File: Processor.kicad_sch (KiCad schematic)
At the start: 36 parts, among them J5 GPIO, SW2 SW_Push, U12 8086_Max_Mode, U13 8284, U14 8087, U15 8089, U16 80130-6, U17 8288, U18 8289, U19 74LS573, U20 74LS245, U21 74LS573, U22 74LS245, U23 74LS573, U24 74LS06, U26 74LS273, U27 74LS273, U28 74LS244, U29 74LS244, U30 74LS32, Y1 15MHz

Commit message: Adjusted Data Bus for 80130
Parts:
- removed unit 3 of U24
- added U34: 74HC00, Package_DIP:DIP-14_W7.62mm, symbol 74xx:74HC00
- J5: footprint (none) -> Connector_PinHeader_2.54mm:PinHeader_2x08_P2.54mm_Vertical
- U15: footprint (none) -> Package_DIP:DIP-40_W15.24mm
- U16: footprint (none) -> Package_DIP:DIP-40_W15.24mm_Socket
- U18, U21, U22, U23, U26, U27, U28: footprint (none) -> Package_DIP:DIP-20_W7.62mm
- U24, U30: footprint (none) -> Package_DIP:DIP-14_W7.62mm
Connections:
- net 5V-18: now also U34.14 (VCC)
- net DEN: now also U34.1
- net GND: now also U34.10, U34.12, U34.13, U34.4, U34.5, U34.7 (GND), U34.9
- net ~{DEN}: now also U34.3
- net ~{LIR}: now reaches U16.24 (~{LIR})
- net ~{ACK}: now reaches U16.25 (~{ACK})
- net ~{ACK}: now also U34.2
- net RDY2: no longer names the net of RN1.3 (R2)
- net RDY2: no longer U13.6 (RDY2)
- new net IORDY: U13.6 (RDY2)

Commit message: assigned all footprints
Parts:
- C3: footprint (none) -> Capacitor_THT:CP_Radial_D6.3mm_P2.50mm
- C4: footprint (none) -> Capacitor_THT:C_Disc_D8.0mm_W2.5mm_P5.00mm
- JP2, JP3, JP4, JP6: footprint (none) -> Connector_PinHeader_2.54mm:PinHeader_1x02_P2.54mm_Vertical
- R3, R4, R5, R6, R7: footprint (none) -> Resistor_THT:R_Axial_DIN0207_L6.3mm_D2.5mm_P7.62mm_Horizontal
- SW2: footprint (none) -> Button_Switch_THT:SW_PUSH_6mm
- U19, U20, U29: footprint (none) -> Package_DIP:DIP-20_W7.62mm
- Y1: footprint (none) -> Crystal:Crystal_HC49-U_Vertical
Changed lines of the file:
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@@
 			)
 		)
-		(property "Footprint" ""
+		(property "Footprint" "Connector_PinHeader_2.54mm:PinHeader_1x02_P2.54mm_Vertical"
 			(at 176.53 194.31 0)
 			(effects
@@
 			)
 		)
-		(property "Footprint" ""
+		(property "Footprint" "Connector_PinHeader_2.54mm:PinHeader_1x02_P2.54mm_Vertical"
 			(at 62.23 114.3 0)
 			(effects
@@
 			)
 		)
-		(property "Footprint" ""
+		(property "Footprint" "Resistor_THT:R_Axial_DIN0207_L6.3mm_D2.5mm_P7.62mm_Horizontal"
 			(at 84.582 30.48 90)
 			(effects
@@
 			)
 		)
-		(property "Footprint" ""
+		(property "Footprint" "Capacitor_THT:C_Disc_D8.0mm_W2.5mm_P5.00mm"
 			(at 65.7352 66.04 0)
 			(effects
@@
 			)
 		)
-		(property "Footprint" ""
+		(property "Footprint" "Resistor_THT:R_Axial_DIN0207_L6.3mm_D2.5mm_P7.62mm_Horizontal"
 			(at 22.352 107.95 90)
 			(effects
@@
 			)
 		)
-		(property "Footprint" ""
+		(property "Footprint" "Connector_PinHeader_2.54mm:PinHeader_1x02_P2.54mm_Vertical"
 			(at 162.2817 212.09 0)
 			(effects
@@
 			)
 		)
-		(property "Footprint" ""
+		(property "Footprint" "Button_Switch_THT:SW_PUSH_6mm"
 			(at 81.28 29.21 0)
 			(effects
@@
 			)
 		)
-		(property "Footprint" ""
+		(property "Footprint" "Crystal:Crystal_HC49-U_Vertical"
 			(at 64.77 69.85 0)
 			(effects
@@
 			)
 		)
-		(property "Footprint" ""
+		(property "Footprint" "Package_DIP:DIP-20_W7.62mm"
 			(at 38.1 166.37 0)
 			(effects
@@
 			)
 		)
-		(property "Footprint" ""
+		(property "Footprint" "Resistor_THT:R_Axial_DIN0207_L6.3mm_D2.5mm_P7.62mm_Horizontal"
 			(at 32.512 107.95 90)
 			(effects
@@
 			)
 		)
-		(property "Footprint" ""
+		(property "Footprint" "Connector_PinHeader_2.54mm:PinHeader_1x02_P2.54mm_Vertical"
 			(at 245.11 118.11 0)
 			(effects
@@
 			)
 		)
-		(property "Footprint" ""
+		(property "Footprint" "Package_DIP:DIP-20_W7.62mm"
 			(at 153.67 331.47 0)
 			(effects
@@
 			)
 		)
-		(property "Footprint" ""
+		(property "Footprint" "Package_DIP:DIP-20_W7.62mm"
 			(at 80.01 166.37 0)
 			(effects
@@
 			)
 		)
-		(property "Footprint" ""
+		(property "Footprint" "Resistor_THT:R_Axial_DIN0207_L6.3mm_D2.5mm_P7.62mm_Horizontal"
 			(at 76.2 67.818 90)
 			(effects
@@
 			)
 		)
-		(property "Footprint" ""
+		(property "Footprint" "Resistor_THT:R_Axial_DIN0207_L6.3mm_D2.5mm_P7.62mm_Horizontal"
 			(at 76.2 71.882 90)
 			(effects
@@
 			)
 		)
-		(property "Footprint" ""
+		(property "Footprint" "Capacitor_THT:CP_Radial_D6.3mm_P2.50mm"
 			(at 91.44 38.1 0)
 			(effects

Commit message: Updated PCB
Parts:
- added C14, C15, C16, C17, C18, C19, C20, C21, C22, C23, C24, C25, C26, C27, C28, C29, C30, C31: 0.1uF, Capacitor_THT:C_Disc_D8.0mm_W2.5mm_P5.00mm, symbol Device:C
- JP2: footprint Connector_PinHeader_2.54mm:PinHeader_1x02_P2.54mm_Vertical -> Connector_PinHeader_2.54mm:PinHeader_1x03_P2.54mm_Vertical
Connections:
- net 5V-18: now also C14.1, C15.1, C16.1, C17.1, C18.1, C19.1, C20.1, C21.1, C22.2, C23.2, C24.2, C25.2, C26.2, C27.2, C28.2, C29.2, C30.2, C31.2
- net GND: now also C14.2, C15.2, C16.2, C17.2, C18.2, C19.2, C20.2, C21.2, C22.1, C23.1, C24.1, C25.1, C26.1, C27.1, C28.1, C29.1, C30.1, C31.1
- net ~{LOCK}: now also JP4.1 (A)
- net at JP4.2 (B): now also U15.29 (~{LOCK})

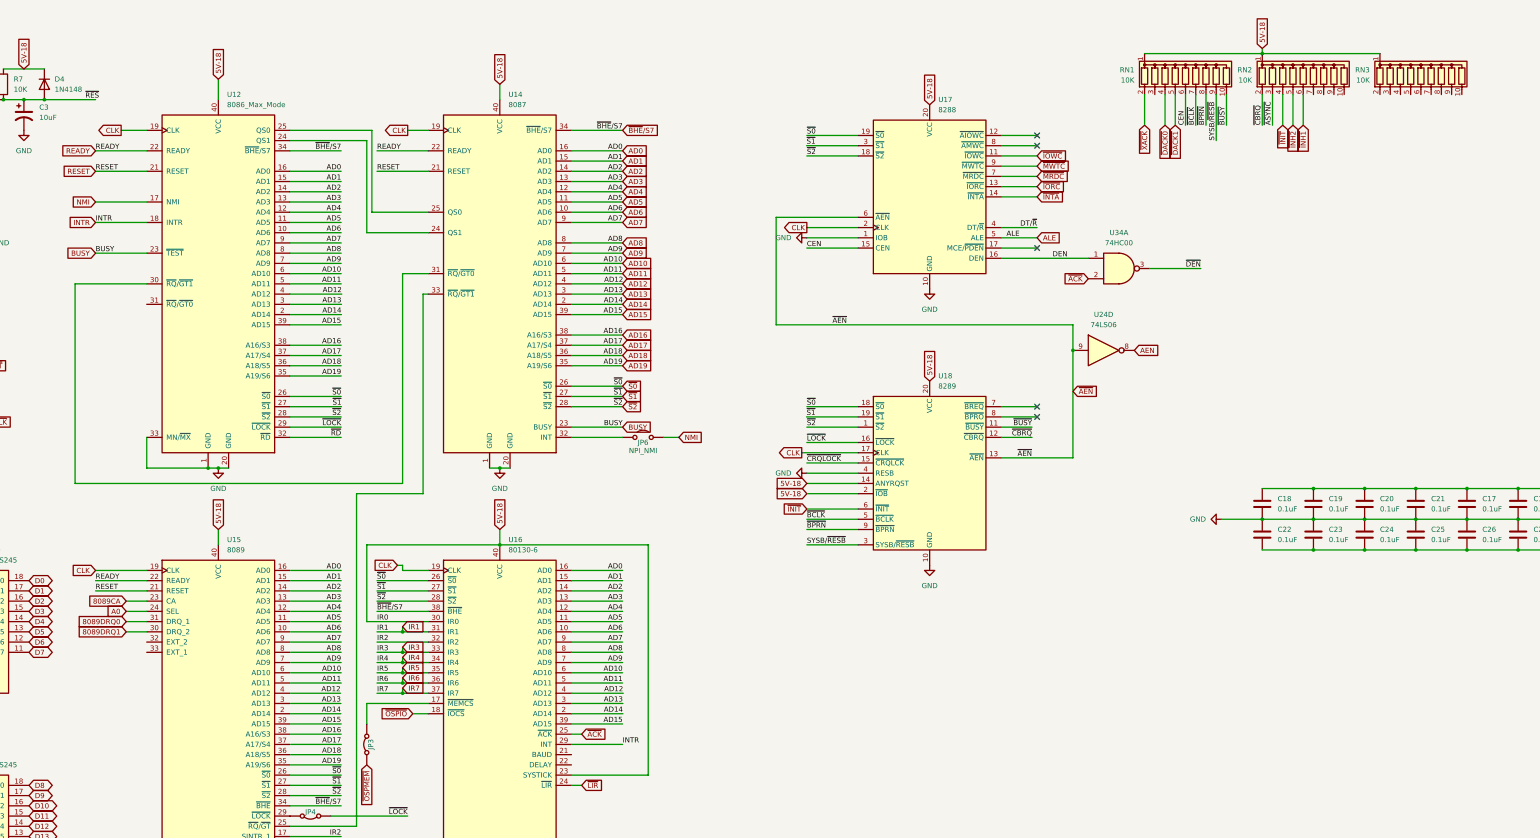
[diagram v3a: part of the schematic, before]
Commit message: Fixed missing nets
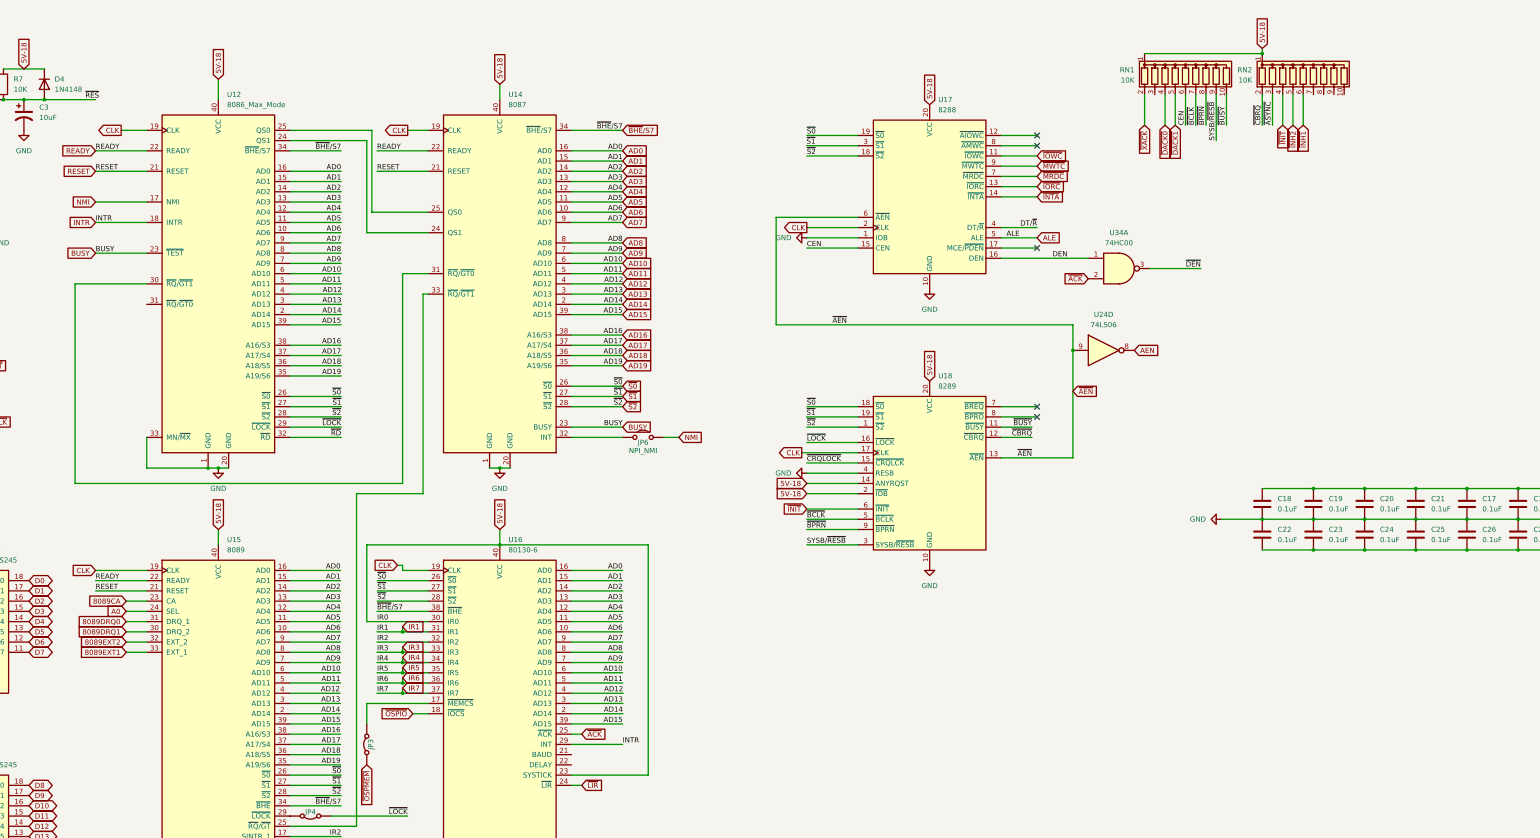
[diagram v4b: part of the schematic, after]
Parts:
- removed RN3: 10K, Resistor_THT:R_Array_SIP10, symbol Device:R_Network09
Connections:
- net AD0: now also U15.16 (AD0)
- net AD1: now also U15.15 (AD1)
- net AD10: now also U15.6 (AD10)
- net AD11: now also U15.5 (AD11)
- net AD12: now also U15.4 (AD12)
- net AD13: now also U15.3 (AD13)
- net AD14: now also U15.2 (AD14)
- net AD15: now also U15.39 (AD15)
- net AD16: now also U15.38 (A16/S3)
- net AD17: now also U15.37 (A17/S4)
- net AD18: now also U15.36 (A18/S5)
- net AD19: now also U15.35 (A19/S6)
- net AD2: now also U15.14 (AD2)
- net AD3: now also U15.13 (AD3)
- net AD4: now also U15.12 (AD4)
- net AD5: now also U15.11 (AD5)
- net AD6: now also U15.10 (AD6)
- net AD7: now also U15.9 (AD7)
- net AD8: now also U15.8 (AD8)
- net AD9: now also U15.7 (AD9)
- net ~{S0}: now also U16.26 (~{S0})
- net ~{S1}: now also U16.27 (~{S1})
- net ~{S2}: now also U16.28 (~{S2})
- net 8089EXT2: now reaches U15.32 (EXT_2)
- net 8089EXT1: now reaches U15.33 (EXT_1)
